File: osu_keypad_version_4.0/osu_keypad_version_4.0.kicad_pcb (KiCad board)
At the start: 2 copper layers, 30 parts, among them J1 AVR-ISP-6, SW1 SW_Push, SW2 RotaryEncoder_Switch, U1 ATmega32U4-A, Y1 16Mhz

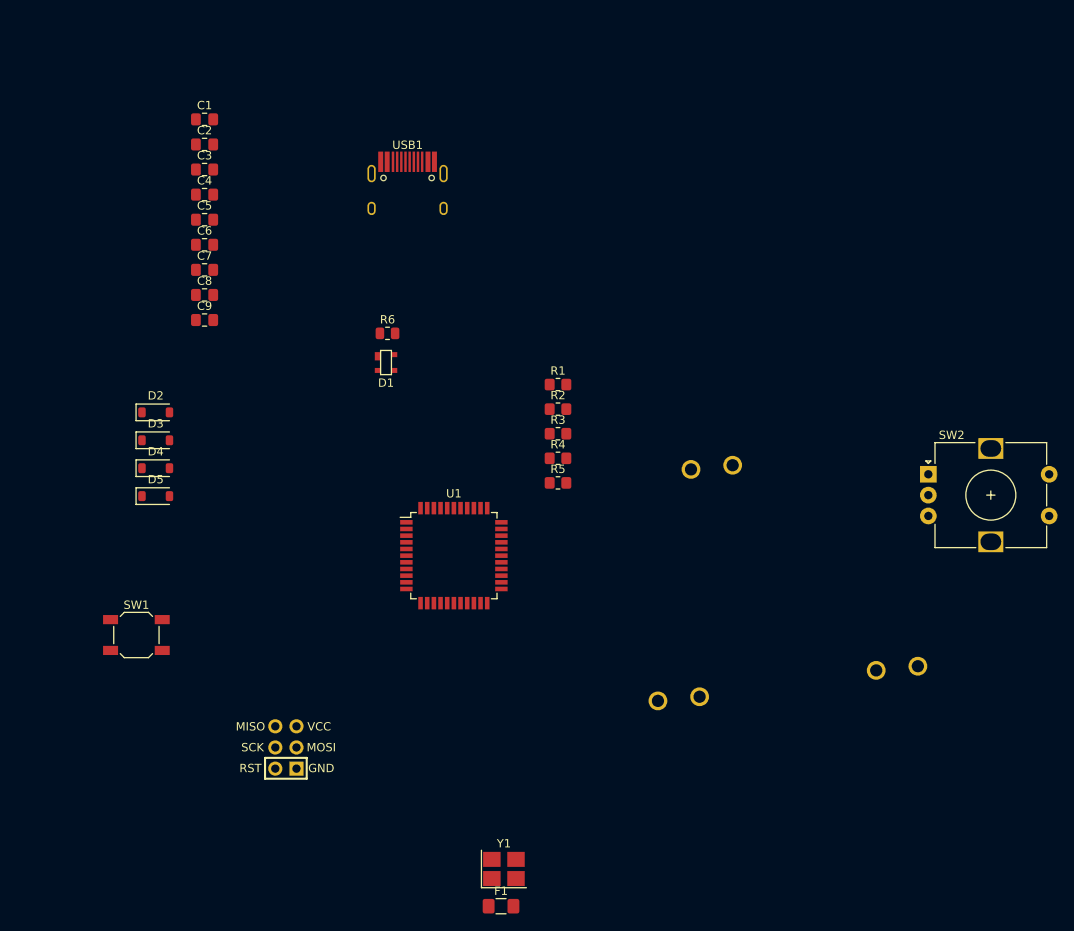
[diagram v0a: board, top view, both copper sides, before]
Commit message: started arranging the footprints
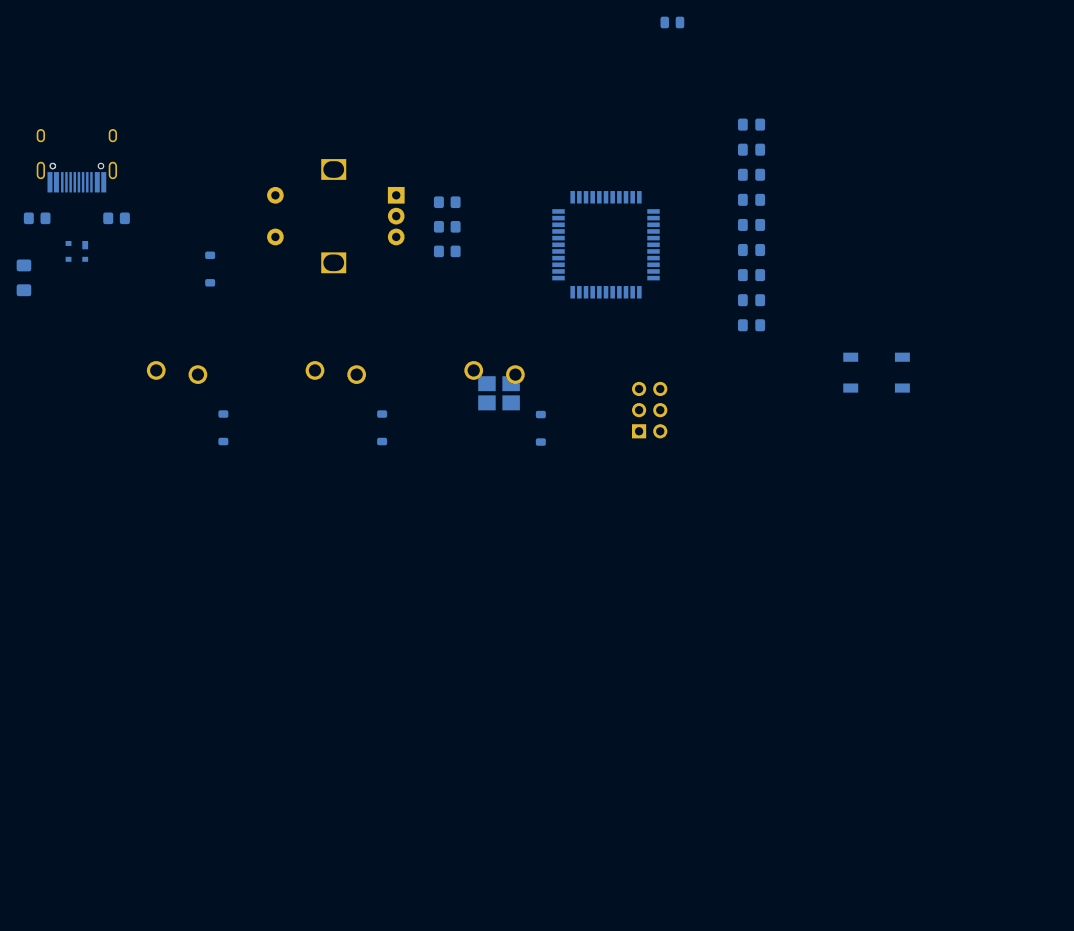
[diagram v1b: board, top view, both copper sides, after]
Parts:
- C1, C2, C3, C4, C5, C6, C7, C8, C9, D1, D2, D3, D4, D5, F1, J1, MX1, MX2, MX3, R1, R2, R3, R4, R5, R6, SW1, SW2, U1, USB1, Y1: moved to B.Cu
- moved F1 94.7 mm to (108.0, 71.4), turned to -90 degrees
- moved SW1 94.2 mm to (210.3, 82.8), turned to 180 degrees
- moved MX3 93.4 mm to (126.3, 87.0), turned to 180 degrees
- moved SW2 72.1 mm to (152.6, 61.5), turned to 180 degrees
- moved R4 68.8 mm to (109.5, 64.3), turned to 180 degrees
- moved C1 65.6 mm to (195.3, 53.0), turned to 180 degrees
- moved C2 65.6 mm to (195.3, 56.1), turned to 180 degrees
- moved C3 65.6 mm to (195.3, 59.1), turned to 180 degrees
- moved C4 65.6 mm to (195.3, 62.1), turned to 180 degrees
- moved C5 65.6 mm to (195.3, 65.1), turned to 180 degrees
- moved C6 65.6 mm to (195.3, 68.1), turned to 180 degrees
- moved C7 65.6 mm to (195.3, 71.1), turned to 180 degrees
- moved C8 65.6 mm to (195.3, 74.1), turned to 180 degrees
- moved C9 65.6 mm to (195.3, 77.1), turned to 180 degrees
- moved R5 61.8 mm to (119.1, 64.3), turned to 180 degrees
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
